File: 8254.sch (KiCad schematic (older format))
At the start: 2 parts

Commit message: minor changes
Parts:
- gave numbers to parts that had none: 2
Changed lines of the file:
@@
 $EndDescr
 $Comp
-L Timer:8254 U?
+L Timer:8254 U2
 U 1 1 60845EE8
 P 5650 3250
-F 0 "U?" H 5650 4431 50  0000 C CNN
+F 0 "U2" H 5650 4431 50  0000 C CNN
 F 1 "8254" H 5650 4340 50  0000 C CNN
 F 2 "Package_DIP:DIP-24_W15.24mm" H 5700 3500 50  0001 C CNN
@@
 $EndComp
 $Comp
-L power:GND #PWR?
+L power:GND #PWR04
 U 1 1 60848002
 P 5650 4250
-F 0 "#PWR?" H 5650 4000 50  0001 C CNN
+F 0 "#PWR04" H 5650 4000 50  0001 C CNN
 F 1 "GND" H 5655 4077 50  0000 C CNN
 F 2 "" H 5650 4250 50  0001 C CNN
@@
 $EndComp
 $Comp
-L power:VCC #PWR?
+L power:VCC #PWR03
 U 1 1 6084836A
 P 5650 1950
-F 0 "#PWR?" H 5650 1800 50  0001 C CNN
+F 0 "#PWR03" H 5650 1800 50  0001 C CNN
 F 1 "VCC" H 5665 2123 50  0000 C CNN
 F 2 "" H 5650 1950 50  0001 C CNN
@@
 	5050 3550 4350 3550
 $Comp
-L Logic_Programmable:PAL16L8 U?
+L Logic_Programmable:PAL16L8 U1
 U 1 1 6084E134
 P 2200 5300
-F 0 "U?" H 2200 6181 50  0000 C CNN
+F 0 "U1" H 2200 6181 50  0000 C CNN
 F 1 "PAL16L8" H 2200 6090 50  0000 C CNN
 F 2 "" H 2200 5300 50  0001 C CNN
@@
 M~IO
 $Comp
-L power:GND #PWR?
+L power:GND #PWR02
 U 1 1 6085575F
 P 2200 5900
-F 0 "#PWR?" H 2200 5650 50  0001 C CNN
+F 0 "#PWR02" H 2200 5650 50  0001 C CNN
 F 1 "GND" H 2205 5727 50  0000 C CNN
 F 2 "" H 2200 5900 50  0001 C CNN
@@
 $EndComp
 $Comp
-L power:VCC #PWR?
+L power:VCC #PWR01
 U 1 1 60855DD6
 P 2200 4200
-F 0 "#PWR?" H 2200 4050 50  0001 C CNN
+F 0 "#PWR01" H 2200 4050 50  0001 C CNN
 F 1 "VCC" H 2215 4373 50  0000 C CNN
 F 2 "" H 2200 4200 50  0001 C CNN
@@
 Wire Wire Line
 	6250 3350 6550 3350
-Wire Bus Line
-	4250 2650 4250 3350
-Wire Bus Line
-	950  3750 950  7050
 Text HLabel 6550 2650 2    50   Output ~ 0
 CLK0
@@
 Text HLabel 950  4150 0    50   Input ~ 0
 A0-A15
+Wire Bus Line
+	4250 2650 4250 3350
+Wire Bus Line
+	950  3750 950  7050
 $EndSCHEMATC

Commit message: updated bus labels and pins
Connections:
- net labels added: A[0:15], D[0:7]
- net labels removed: A0, A0-A15, A1, A10, A11, A12, A13, A14, A15, A2, A3, A4, A5, A6, A7, A8, A9, D0, D0-D7, D1, D2, D3, D4, D5, D6, D7
- no-connect marks 0 -> 1
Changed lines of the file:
@@
 Wire Wire Line
 	5050 3550 4350 3550
-$Comp
-L Logic_Programmable:PAL16L8 U1
-U 1 1 6084E134
-P 2200 5300
-F 0 "U1" H 2200 6181 50  0000 C CNN
-F 1 "PAL16L8" H 2200 6090 50  0000 C CNN
-F 2 "" H 2200 5300 50  0001 C CNN
-F 3 "" H 2200 5300 50  0001 C CNN
-	1    2200 5300
-	1    0    0    -1
-$EndComp
 Entry Wire Line
 	4250 2750 4350 2650
@@
 	4250 2650 4350 2550
 Text HLabel 4250 2650 0    50   Input ~ 0
-D0-D7
+D[0:7]
 Text HLabel 4350 3450 0    50   Input ~ 0
 ~RD
 Text HLabel 4350 3550 0    50   Input ~ 0
 ~WR
-Text HLabel 1050 3650 0    50   Input ~ 0
-A1
-Text HLabel 1050 3750 0    50   Input ~ 0
-A2
-Text HLabel 4350 2550 2    50   Input ~ 0
-D0
-Text HLabel 4350 2650 2    50   Input ~ 0
-D1
-Text HLabel 4350 2750 2    50   Input ~ 0
-D2
-Text HLabel 4350 2850 2    50   Input ~ 0
-D3
-Text HLabel 4350 2950 2    50   Input ~ 0
-D4
-Text HLabel 4350 3050 2    50   Input ~ 0
-D5
-Text HLabel 4350 3150 2    50   Input ~ 0
-D6
-Text HLabel 4350 3250 2    50   Input ~ 0
-D7
 Text HLabel 1200 4800 0    50   Input ~ 0
 M~IO
@@
 Wire Wire Line
 	2200 4600 2200 4200
-Text HLabel 1050 4900 0    50   Input ~ 0
-A0
-Text HLabel 1050 5000 0    50   Input ~ 0
-A3
-Text HLabel 1050 5100 0    50   Input ~ 0
-A4
-Text HLabel 1050 5200 0    50   Input ~ 0
-A5
-Text HLabel 1050 5300 0    50   Input ~ 0
-A6
-Text HLabel 1050 5400 0    50   Input ~ 0
-A7
-Text HLabel 1050 5500 0    50   Input ~ 0
-A8
-Text HLabel 1050 5600 0    50   Input ~ 0
-A9
-Text HLabel 1050 5700 0    50   Input ~ 0
-A10
 Text HLabel 3850 3950 0    50   Input ~ 0
 ~WAIT2
@@
 Wire Wire Line
 	3750 6950 1050 6950
-Text HLabel 1050 6200 0    50   Input ~ 0
-A11
-Text HLabel 1050 6350 0    50   Input ~ 0
-A12
-Text HLabel 1050 6550 0    50   Input ~ 0
-A13
-Text HLabel 1050 6750 0    50   Input ~ 0
-A14
-Text HLabel 1050 6950 0    50   Input ~ 0
-A15
 Wire Wire Line
 	1050 3650 5050 3650
@@
 G2
 Text HLabel 950  4150 0    50   Input ~ 0
-A0-A15
+A[0:15]
+$Comp
+L Logic_Programmable:PAL16L8 U1
+U 1 1 6084E134
+P 2200 5300
+F 0 "U1" H 2200 6181 50  0000 C CNN
+F 1 "PAL16L8" H 2200 6090 50  0000 C CNN
+F 2 "" H 2200 5300 50  0001 C CNN
+F 3 "" H 2200 5300 50  0001 C CNN
+	1    2200 5300
+	1    0    0    -1
+$EndComp
+NoConn ~ 2700 5500
 Wire Bus Line
 	4250 2650 4250 3350

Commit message: updated counters
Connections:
- net labels added: A0, A1, COUNTER1, COUNTER2, COUNTER3
- net labels removed: IR1, OUT0, OUT2
- wire segments 54 -> 52
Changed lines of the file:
@@
 Wire Wire Line
 	3750 6950 1050 6950
-Wire Wire Line
-	1050 3650 5050 3650
-Wire Wire Line
-	1050 3750 5050 3750
-Entry Wire Line
-	950  3750 1050 3650
-Entry Wire Line
-	950  3850 1050 3750
 Entry Wire Line
 	950  5000 1050 4900
@@
 	6250 2850 6550 2850
 Text HLabel 6550 2850 2    50   Output ~ 0
-OUT0
+COUNTER1
 Text HLabel 6550 3850 2    50   Output ~ 0
-OUT2
-Text HLabel 6550 3350 2    50   Output ~ 0
-IR1
+COUNTER3
 Wire Wire Line
 	6250 2650 6550 2650
@@
 Text HLabel 6550 3750 2    50   Output ~ 0
 G2
-Text HLabel 950  4150 0    50   Input ~ 0
+Text HLabel 950  5050 0    50   Input ~ 0
 A[0:15]
 $Comp
@@
 	4250 2650 4250 3350
 Wire Bus Line
-	950  3750 950  7050
+	950  5000 950  7050
+Text HLabel 5050 3650 0    50   Input ~ 0
+A0
+Text HLabel 5050 3750 0    50   Input ~ 0
+A1
+Text HLabel 6550 3350 2    50   Output ~ 0
+COUNTER2
 $EndSCHEMATC

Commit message: updated pins instead of busses
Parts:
- added J2: Conn_01x08_Female, symbol Connector:Conn_01x08_Female
- renumbered U1 to U26, U2 to U27
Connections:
- net labels added: A10, A11, A12, A13, A14, A15, A3, A4, A5, A6, A7, A8, A9, D0, D1, D2, D3, D4, D5, D6, D7
- net labels removed: A[0:15], CLK0, CLK1, CLK2, COUNTER1, COUNTER3, D[0:7], G0, G1, G2, ~WAIT2
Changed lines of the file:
@@
 $EndDescr
 $Comp
-L Timer:8254 U2
+L Timer:8254 U27
 U 1 1 60845EE8
 P 5650 3250
-F 0 "U2" H 5650 4431 50  0000 C CNN
+F 0 "U27" H 5650 4431 50  0000 C CNN
 F 1 "8254" H 5650 4340 50  0000 C CNN
 F 2 "Package_DIP:DIP-24_W15.24mm" H 5700 3500 50  0001 C CNN
@@
 $EndComp
 $Comp
-L power:GND #PWR04
+L power:GND #PWR045
 U 1 1 60848002
 P 5650 4250
-F 0 "#PWR04" H 5650 4000 50  0001 C CNN
+F 0 "#PWR045" H 5650 4000 50  0001 C CNN
 F 1 "GND" H 5655 4077 50  0000 C CNN
 F 2 "" H 5650 4250 50  0001 C CNN
@@
 $EndComp
 $Comp
-L power:VCC #PWR03
+L power:VCC #PWR044
 U 1 1 6084836A
 P 5650 1950
-F 0 "#PWR03" H 5650 1800 50  0001 C CNN
+F 0 "#PWR044" H 5650 1800 50  0001 C CNN
 F 1 "VCC" H 5665 2123 50  0000 C CNN
 F 2 "" H 5650 1950 50  0001 C CNN
@@
 Wire Wire Line
 	5050 3550 4350 3550
-Entry Wire Line
-	4250 2750 4350 2650
-Entry Wire Line
-	4250 2850 4350 2750
-Entry Wire Line
-	4250 2950 4350 2850
-Entry Wire Line
-	4250 3050 4350 2950
-Entry Wire Line
-	4250 3250 4350 3150
-Entry Wire Line
-	4250 3350 4350 3250
-Entry Wire Line
-	4250 3150 4350 3050
-Entry Wire Line
-	4250 2650 4350 2550
-Text HLabel 4250 2650 0    50   Input ~ 0
-D[0:7]
 Text HLabel 4350 3450 0    50   Input ~ 0
 ~RD
 Text HLabel 4350 3550 0    50   Input ~ 0
 ~WR
-Text HLabel 1200 4800 0    50   Input ~ 0
-M~IO
-$Comp
-L power:GND #PWR02
+$Comp
+L power:GND #PWR043
 U 1 1 6085575F
 P 2200 5900
-F 0 "#PWR02" H 2200 5650 50  0001 C CNN
+F 0 "#PWR043" H 2200 5650 50  0001 C CNN
 F 1 "GND" H 2205 5727 50  0000 C CNN
 F 2 "" H 2200 5900 50  0001 C CNN
@@
 $EndComp
 $Comp
-L power:VCC #PWR01
+L power:VCC #PWR042
 U 1 1 60855DD6
 P 2200 4200
-F 0 "#PWR01" H 2200 4050 50  0001 C CNN
+F 0 "#PWR042" H 2200 4050 50  0001 C CNN
 F 1 "VCC" H 2215 4373 50  0000 C CNN
 F 2 "" H 2200 4200 50  0001 C CNN
@@
 Wire Wire Line
 	2200 4600 2200 4200
-Text HLabel 3850 3950 0    50   Input ~ 0
-~WAIT2
 Wire Wire Line
 	5050 3950 4700 3950
@@
 Wire Wire Line
 	4700 4900 4700 4800
-Connection ~ 4700 3950
-Wire Wire Line
-	4700 3950 3850 3950
 Wire Wire Line
 	2700 4800 4700 4800
@@
 	4700 4800 4700 3950
 Wire Wire Line
-	2700 5400 3000 5400
-Wire Wire Line
-	3000 5400 3000 6200
-Wire Wire Line
-	3000 6200 1050 6200
-Wire Wire Line
-	3150 5300 3150 6350
-Wire Wire Line
-	3150 6350 1050 6350
-Wire Wire Line
-	2700 5300 3150 5300
-Wire Wire Line
-	3350 5200 3350 6550
-Wire Wire Line
-	3350 6550 1050 6550
-Wire Wire Line
-	2700 5200 3350 5200
-Wire Wire Line
-	3550 5100 3550 6750
-Wire Wire Line
-	3550 6750 1050 6750
-Wire Wire Line
-	2700 5100 3550 5100
-Wire Wire Line
-	2700 5000 3750 5000
-Wire Wire Line
-	3750 5000 3750 6950
-Wire Wire Line
-	3750 6950 1050 6950
-Entry Wire Line
-	950  5000 1050 4900
-Entry Wire Line
-	950  5100 1050 5000
-Entry Wire Line
-	950  5200 1050 5100
-Entry Wire Line
-	950  5300 1050 5200
-Entry Wire Line
-	950  5400 1050 5300
-Entry Wire Line
-	950  5500 1050 5400
-Entry Wire Line
-	950  5600 1050 5500
-Entry Wire Line
-	950  5700 1050 5600
-Entry Wire Line
-	950  5800 1050 5700
-Entry Wire Line
-	950  6300 1050 6200
-Entry Wire Line
-	950  6450 1050 6350
-Entry Wire Line
-	950  6650 1050 6550
-Entry Wire Line
-	950  6850 1050 6750
-Entry Wire Line
-	950  7050 1050 6950
-Wire Wire Line
 	1050 4900 1700 4900
 Wire Wire Line
@@
 Wire Wire Line
 	1700 4800 1200 4800
-Wire Wire Line
-	6250 2850 6550 2850
-Text HLabel 6550 2850 2    50   Output ~ 0
-COUNTER1
-Text HLabel 6550 3850 2    50   Output ~ 0
-COUNTER3
-Wire Wire Line
-	6250 2650 6550 2650
-Wire Wire Line
-	6250 2750 6550 2750
-Wire Wire Line
-	6250 3150 6550 3150
-Wire Wire Line
-	6250 3250 6550 3250
-Wire Wire Line
-	6250 3650 6550 3650
-Wire Wire Line
-	6250 3750 6550 3750
-Wire Wire Line
-	6250 3850 6550 3850
-Wire Wire Line
-	6250 3350 6550 3350
-Text HLabel 6550 2650 2    50   Output ~ 0
-CLK0
-Text HLabel 6550 3150 2    50   Output ~ 0
-CLK1
-Text HLabel 6550 3650 2    50   Output ~ 0
-CLK2
-Text HLabel 6550 2750 2    50   Output ~ 0
-G0
-Text HLabel 6550 3250 2    50   Output ~ 0
-G1
-Text HLabel 6550 3750 2    50   Output ~ 0
-G2
-Text HLabel 950  5050 0    50   Input ~ 0
-A[0:15]
-$Comp
-L Logic_Programmable:PAL16L8 U1
+$Comp
+L Logic_Programmable:PAL16L8 U26
 U 1 1 6084E134
 P 2200 5300
-F 0 "U1" H 2200 6181 50  0000 C CNN
+F 0 "U26" H 2200 6181 50  0000 C CNN
 F 1 "PAL16L8" H 2200 6090 50  0000 C CNN
 F 2 "" H 2200 5300 50  0001 C CNN
@@
 $EndComp
 NoConn ~ 2700 5500
-Wire Bus Line
-	4250 2650 4250 3350
-Wire Bus Line
-	950  5000 950  7050
 Text HLabel 5050 3650 0    50   Input ~ 0
 A0
 Text HLabel 5050 3750 0    50   Input ~ 0
 A1
-Text HLabel 6550 3350 2    50   Output ~ 0
+Text HLabel 6250 3350 2    50   Output ~ 0
 COUNTER2
+$Comp
+L Connector:Conn_01x08_Female J2
+U 1 1 60B4C76F
+P 7850 3150
+F 0 "J2" H 7878 3126 50  0000 L CNN
+F 1 "Conn_01x08_Female" H 7878 3035 50  0000 L CNN
+F 2 "" H 7850 3150 50  0001 C CNN
+F 3 "~" H 7850 3150 50  0001 C CNN
+	1    7850 3150
+	1    0    0    -1
+$EndComp
+Wire Wire Line
+	6250 2650 7550 2650
+Wire Wire Line
+	7550 2650 7550 2850
+Wire Wire Line
+	7550 2850 7650 2850
+Wire Wire Line
+	6250 2750 7500 2750
+Wire Wire Line
+	7500 2750 7500 2950
+Wire Wire Line
+	7500 2950 7650 2950
+Wire Wire Line
+	6250 2850 7450 2850
+Wire Wire Line
+	7450 2850 7450 3050
+Wire Wire Line
+	7450 3050 7650 3050
+Wire Wire Line
+	6250 3150 7650 3150
+Wire Wire Line
+	6250 3250 7650 3250
+Wire Wire Line
+	6250 3850 7550 3850
+Wire Wire Line
+	7550 3850 7550 3550
+Wire Wire Line
+	7550 3550 7650 3550
+Wire Wire Line
+	6250 3750 7500 3750
+Wire Wire Line
+	7500 3750 7500 3450
+Wire Wire Line
+	7500 3450 7650 3450
+Wire Wire Line
+	6250 3650 7450 3650
+Wire Wire Line
+	7450 3650 7450 3350
+Wire Wire Line
+	7450 3350 7650 3350
+Text HLabel 4350 2550 0    50   Input ~ 0
+D0
+Text HLabel 4350 2650 0    50   Input ~ 0
+D1
+Text HLabel 4350 2750 0    50   Input ~ 0
+D2
+Text HLabel 4350 2850 0    50   Input ~ 0
+D3
+Text HLabel 4350 2950 0    50   Input ~ 0
+D4
+Text HLabel 4350 3050 0    50   Input ~ 0
+D5
+Text HLabel 4350 3150 0    50   Input ~ 0
+D6
+Text HLabel 4350 3250 0    50   Input ~ 0
+D7
+Text HLabel 1200 4800 0    50   Input ~ 0
+M~IO
+Text HLabel 1050 4900 0    50   Input ~ 0
+A0
+Wire Wire Line
+	2700 5000 3000 5000
+Wire Wire Line
+	2700 5100 3000 5100
+Wire Wire Line
+	2700 5200 3000 5200
+Wire Wire Line
+	2700 5300 3000 5300
+Wire Wire Line
+	2700 5400 3000 5400
+Text HLabel 3000 5000 2    50   Input ~ 0
+A15
+Text HLabel 3000 5100 2    50   Input ~ 0
+A14
+Text HLabel 3000 5200 2    50   Input ~ 0
+A13
+Text HLabel 3000 5300 2    50   Input ~ 0
+A12
+Text HLabel 3000 5400 2    50   Input ~ 0
+A11
+Text HLabel 1050 5000 0    50   Input ~ 0
+A3
+Text HLabel 1050 5100 0    50   Input ~ 0
+A4
+Text HLabel 1050 5200 0    50   Input ~ 0
+A5
+Text HLabel 1050 5300 0    50   Input ~ 0
+A6
+Text HLabel 1050 5400 0    50   Input ~ 0
+A7
+Text HLabel 1050 5500 0    50   Input ~ 0
+A8
+Text HLabel 1050 5600 0    50   Input ~ 0
+A9
+Text HLabel 1050 5700 0    50   Input ~ 0
+A10
 $EndSCHEMATC

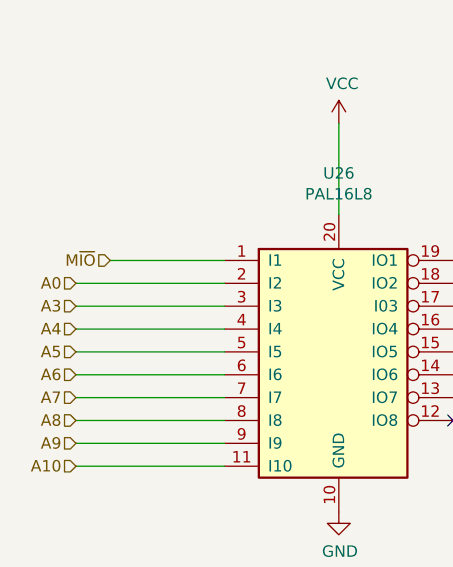
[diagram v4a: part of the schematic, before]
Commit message: added A2
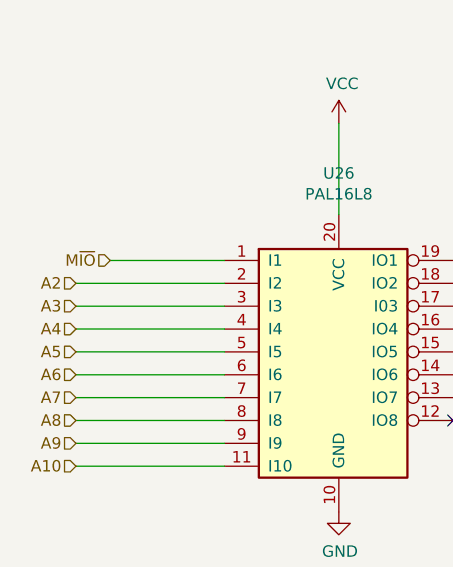
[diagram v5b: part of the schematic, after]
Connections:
- net labels added: A2
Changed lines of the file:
@@
 M~IO
 Text HLabel 1050 4900 0    50   Input ~ 0
-A0
+A2
 Wire Wire Line
 	2700 5000 3000 5000

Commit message: annotations
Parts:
- added Counter_Resistor: 10000, symbol Device:R_Small_US
- renumbered U27 to Counter, U26 to Counter_Decode, J2 to Counter_Header
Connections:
- net labels added: +5V, CLK
- wire segments 52 -> 58
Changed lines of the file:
@@
 $EndDescr
 $Comp
-L Timer:8254 U27
+L Timer:8254 Counter
 U 1 1 60845EE8
 P 5650 3250
-F 0 "U27" H 5650 4431 50  0000 C CNN
+F 0 "Counter" H 5650 4431 50  0000 C CNN
 F 1 "8254" H 5650 4340 50  0000 C CNN
 F 2 "Package_DIP:DIP-24_W15.24mm" H 5700 3500 50  0001 C CNN
@@
 $EndComp
 $Comp
-L power:GND #PWR045
-U 1 1 60848002
-P 5650 4250
-F 0 "#PWR045" H 5650 4000 50  0001 C CNN
-F 1 "GND" H 5655 4077 50  0000 C CNN
-F 2 "" H 5650 4250 50  0001 C CNN
-F 3 "" H 5650 4250 50  0001 C CNN
-	1    5650 4250
-	1    0    0    -1
-$EndComp
-$Comp
 L power:VCC #PWR044
 U 1 1 6084836A
-P 5650 1950
-F 0 "#PWR044" H 5650 1800 50  0001 C CNN
-F 1 "VCC" H 5665 2123 50  0000 C CNN
-F 2 "" H 5650 1950 50  0001 C CNN
-F 3 "" H 5650 1950 50  0001 C CNN
-	1    5650 1950
-	1    0    0    -1
-$EndComp
-Wire Wire Line
-	5650 2250 5650 1950
+P 5650 1600
+F 0 "#PWR044" H 5650 1450 50  0001 C CNN
+F 1 "VCC" H 5665 1773 50  0000 C CNN
+F 2 "" H 5650 1600 50  0001 C CNN
+F 3 "" H 5650 1600 50  0001 C CNN
+	1    5650 1600
+	1    0    0    -1
+$EndComp
 Wire Wire Line
 	5050 2550 4350 2550
@@
 L power:GND #PWR043
 U 1 1 6085575F
-P 2200 5900
-F 0 "#PWR043" H 2200 5650 50  0001 C CNN
-F 1 "GND" H 2205 5727 50  0000 C CNN
-F 2 "" H 2200 5900 50  0001 C CNN
-F 3 "" H 2200 5900 50  0001 C CNN
-	1    2200 5900
-	1    0    0    -1
-$EndComp
-$Comp
-L power:VCC #PWR042
-U 1 1 60855DD6
-P 2200 4200
-F 0 "#PWR042" H 2200 4050 50  0001 C CNN
-F 1 "VCC" H 2215 4373 50  0000 C CNN
-F 2 "" H 2200 4200 50  0001 C CNN
-F 3 "" H 2200 4200 50  0001 C CNN
-	1    2200 4200
-	1    0    0    -1
-$EndComp
-Wire Wire Line
-	2200 4600 2200 4200
+P 2200 6200
+F 0 "#PWR043" H 2200 5950 50  0001 C CNN
+F 1 "GND" H 2205 6027 50  0000 C CNN
+F 2 "" H 2200 6200 50  0001 C CNN
+F 3 "" H 2200 6200 50  0001 C CNN
+	1    2200 6200
+	1    0    0    -1
+$EndComp
 Wire Wire Line
 	5050 3950 4700 3950
@@
 	1700 4800 1200 4800
 $Comp
-L Logic_Programmable:PAL16L8 U26
+L Logic_Programmable:PAL16L8 Counter_Decode
 U 1 1 6084E134
 P 2200 5300
-F 0 "U26" H 2200 6181 50  0000 C CNN
+F 0 "Counter_Decode" H 2200 6181 50  0000 C CNN
 F 1 "PAL16L8" H 2200 6090 50  0000 C CNN
 F 2 "" H 2200 5300 50  0001 C CNN
@@
 Text HLabel 6250 3350 2    50   Output ~ 0
 COUNTER2
-$Comp
-L Connector:Conn_01x08_Female J2
-U 1 1 60B4C76F
-P 7850 3150
-F 0 "J2" H 7878 3126 50  0000 L CNN
-F 1 "Conn_01x08_Female" H 7878 3035 50  0000 L CNN
-F 2 "" H 7850 3150 50  0001 C CNN
-F 3 "~" H 7850 3150 50  0001 C CNN
-	1    7850 3150
-	1    0    0    -1
-$EndComp
 Wire Wire Line
 	6250 2650 7550 2650
@@
 Wire Wire Line
 	7450 3050 7650 3050
-Wire Wire Line
-	6250 3150 7650 3150
-Wire Wire Line
-	6250 3250 7650 3250
 Wire Wire Line
 	6250 3850 7550 3850
@@
 Text HLabel 1050 5700 0    50   Input ~ 0
 A10
+$Comp
+L power:+5V #PWR0133
+U 1 1 61A121ED
+P 6900 3250
+F 0 "#PWR0133" H 6900 3100 50  0001 C CNN
+F 1 "+5V" V 6915 3378 50  0000 L CNN
+F 2 "" H 6900 3250 50  0001 C CNN
+F 3 "" H 6900 3250 50  0001 C CNN
+	1    6900 3250
+	0    1    1    0
+$EndComp
+$Comp
+L Device:R_Small_US Counter_Resistor
+U 1 1 61A1330B
+P 6650 3250
+F 0 "Counter_Resistor" V 6445 3250 50  0000 C CNN
+F 1 "10000" V 6536 3250 50  0000 C CNN
+F 2 "" H 6650 3250 50  0001 C CNN
+F 3 "~" H 6650 3250 50  0001 C CNN
+	1    6650 3250
+	0    1    1    0
+$EndComp
+Wire Wire Line
+	6900 3250 6750 3250
+Wire Wire Line
+	6550 3250 6250 3250
+Text HLabel 6250 3150 2    50   Input ~ 0
+CLK
+Wire Wire Line
+	2200 5900 2200 6050
+Wire Wire Line
+	5650 4250 5650 6050
+Wire Wire Line
+	5650 6050 2200 6050
+Connection ~ 2200 6050
+Wire Wire Line
+	2200 1900 5650 1900
+Wire Wire Line
+	2200 1900 2200 4600
+Connection ~ 5650 1900
+Wire Wire Line
+	5650 1900 5650 2250
+Wire Wire Line
+	2200 6050 2200 6200
+Wire Wire Line
+	5650 1600 5650 1900
+$Comp
+L Connector:Conn_01x08_Female Counter_Header
+U 1 1 60B4C76F
+P 7850 3150
+F 0 "Counter_Header" H 7878 3126 50  0000 L CNN
+F 1 "Conn_01x08_Female" H 7878 3035 50  0000 L CNN
+F 2 "" H 7850 3150 50  0001 C CNN
+F 3 "~" H 7850 3150 50  0001 C CNN
+	1    7850 3150
+	1    0    0    -1
+$EndComp
 $EndSCHEMATC
